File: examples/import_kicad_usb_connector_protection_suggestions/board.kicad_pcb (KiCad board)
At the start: 4 parts, among them J1 USB2_CONNECTOR

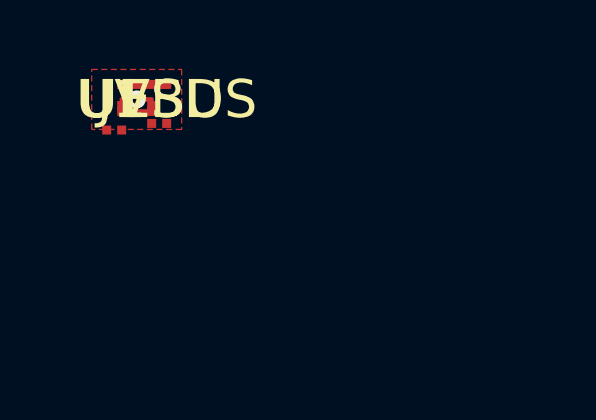
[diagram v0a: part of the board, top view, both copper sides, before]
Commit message: Import KiCad board outline evidence
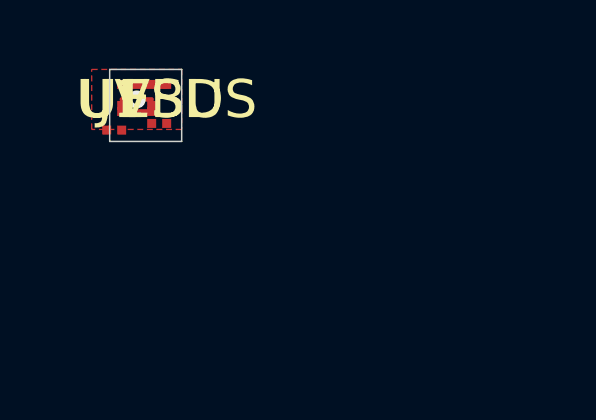
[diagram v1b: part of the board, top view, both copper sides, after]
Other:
- board outline added: 2.4 x 2.4 mm
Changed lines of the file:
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@@
     (constraint length (max 25mm))
     (constraint skew (max 0.5mm) within_diff_pairs))
+  (gr_line (start -0.4 -1.0) (end 2.0 -1.0) (stroke (width 0.05) (type solid)) (layer "Edge.Cuts"))
+  (gr_line (start 2.0 -1.0) (end 2.0 1.4) (stroke (width 0.05) (type solid)) (layer "Edge.Cuts"))
+  (gr_line (start 2.0 1.4) (end -0.4 1.4) (stroke (width 0.05) (type solid)) (layer "Edge.Cuts"))
+  (gr_line (start -0.4 1.4) (end -0.4 -1.0) (stroke (width 0.05) (type solid)) (layer "Edge.Cuts"))
   (footprint "Connector:USB2" (layer "F.Cu")
     (at 0 0 0)
